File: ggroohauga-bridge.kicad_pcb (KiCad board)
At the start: 2 copper layers, 98.5 x 31 mm, 11 parts

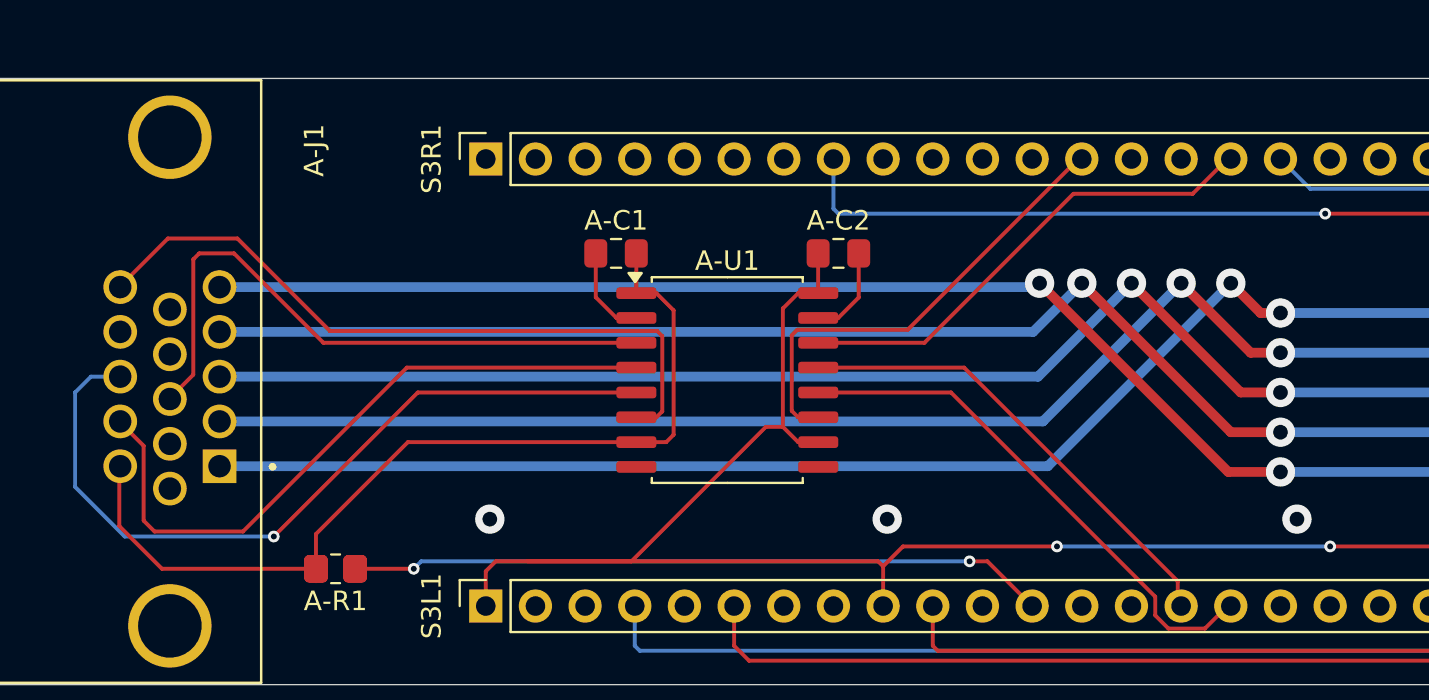
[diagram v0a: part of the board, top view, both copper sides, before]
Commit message: Add pull-up resistors to amplifier detect and RX inputs
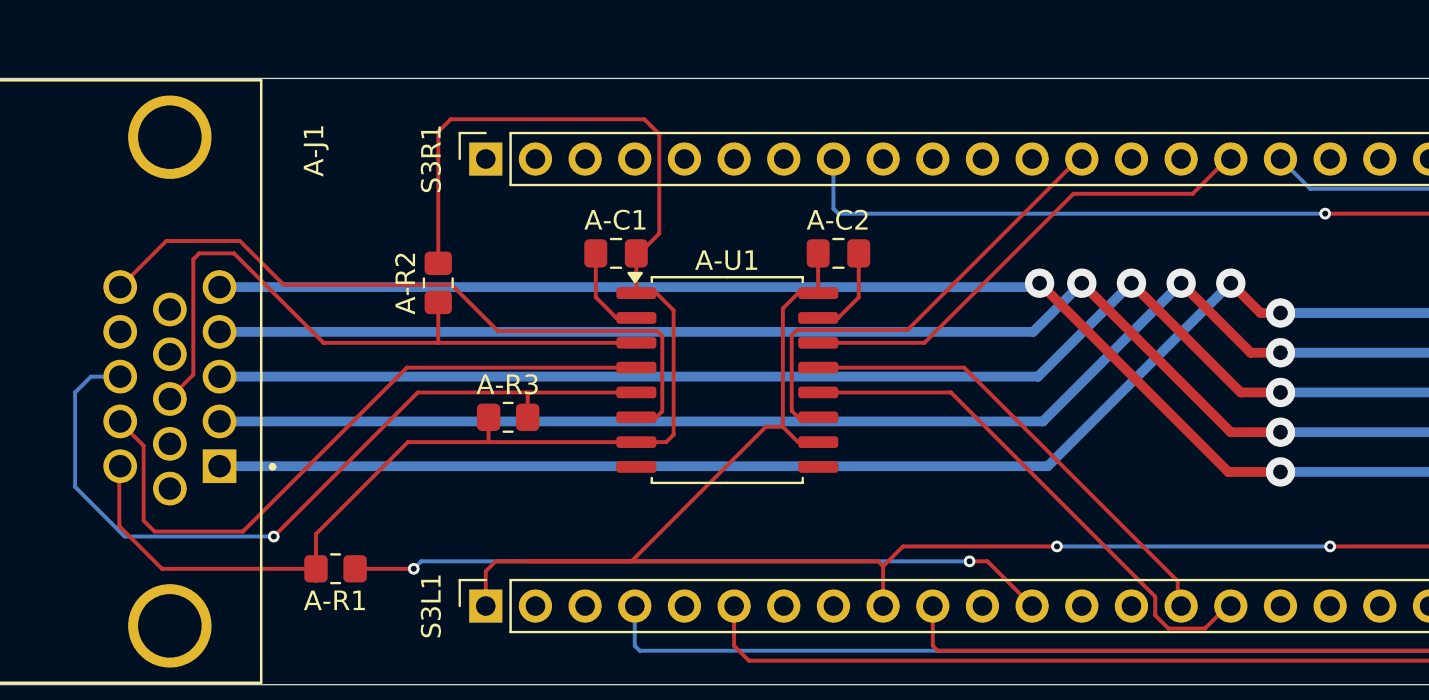
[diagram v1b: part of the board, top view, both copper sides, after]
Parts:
- removed ? (x2): , 
- added A-R2: 10kΩ, Resistor_SMD:R_0805_2012Metric_Pad1.20x1.40mm_HandSolder, F.Cu at (79.1, 60.9)
- added A-R3: 10kΩ, Resistor_SMD:R_0805_2012Metric_Pad1.20x1.40mm_HandSolder, F.Cu at (82.7, 67.8)
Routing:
- net /Common/AMP_POWER_IN: track 47.5 -> 73.9 mm
- net /Common/AMP_DETECT: track 32.3 -> 34.4 mm
- net /Common/AMP_RX: track 40.2 -> 41.5 mm
- net GND: vias 3 -> 0

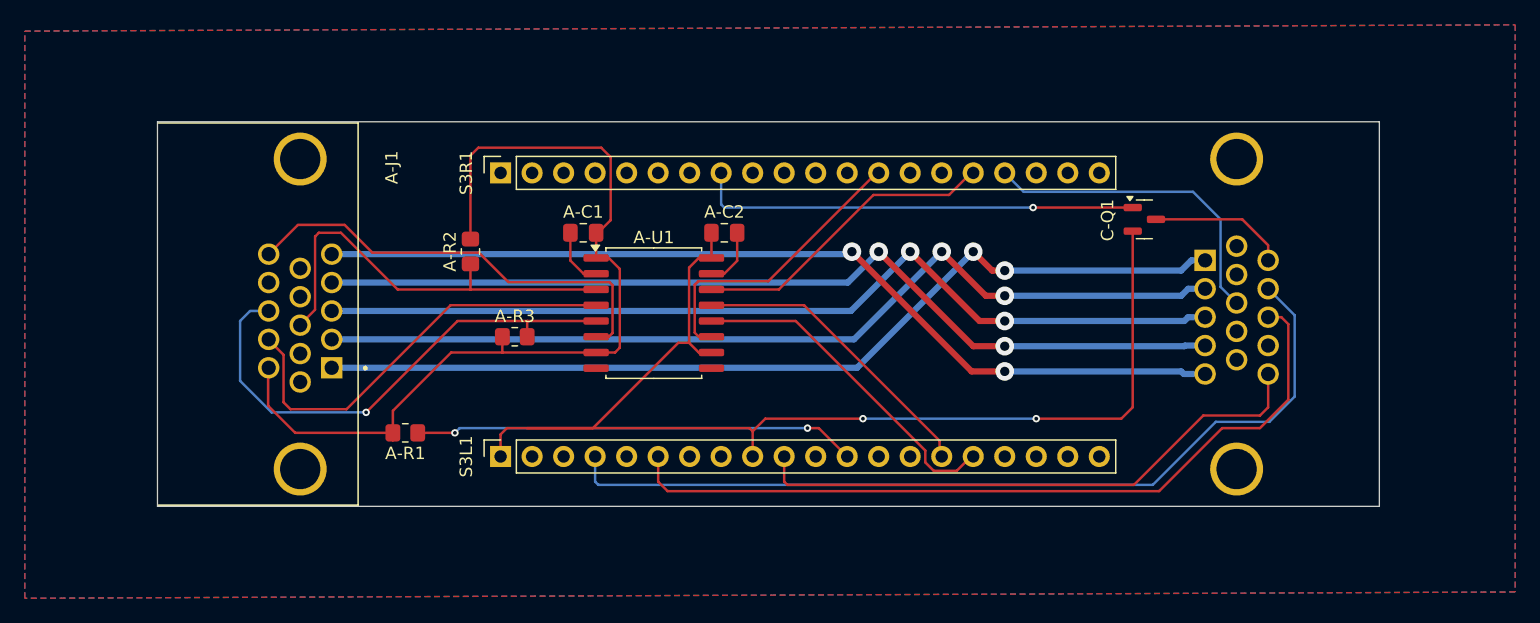
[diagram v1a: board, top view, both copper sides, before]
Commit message: Use consistent position of audio vias and rear silkscreen
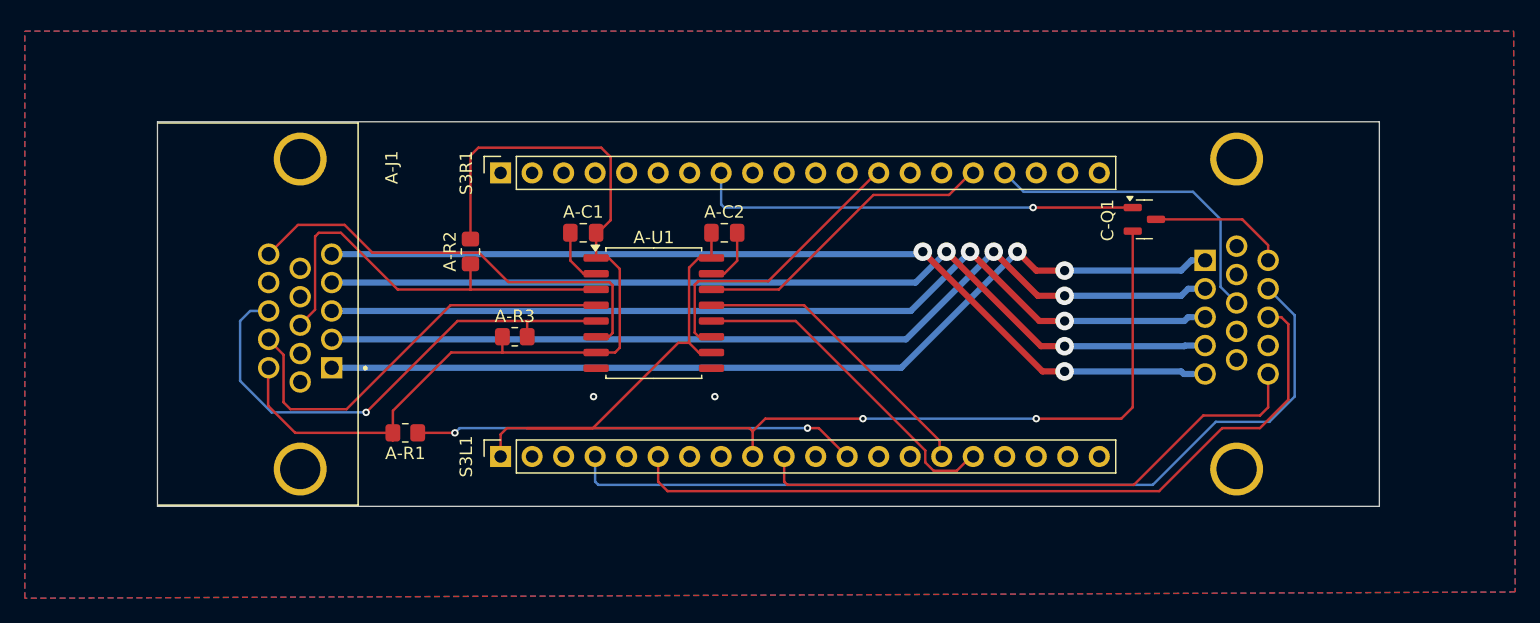
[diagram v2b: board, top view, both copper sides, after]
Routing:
- net GND: vias 0 -> 2
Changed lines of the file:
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@@
 	)
 	(gr_text "JLCJLCJLCJLC"
-		(at 132.366 58.42 90)
+		(at 134.144 58.42 90)
 		(layer "B.SilkS")
 		(effects
@@
 	)
 	(gr_text "urn:oid:1.3.6.1.4.1.39777.1.3.1.3.3\nhttps://github.com/nomis/ggroohauga-pcb\n(bridge)\n"
-		(at 120.65 66.04 0)
+		(at 123.825 66.04 0)
 		(layer "B.SilkS")
 		(effects
@@
 	)
 	(segment
-		(start 112.014 60.96)
-		(end 119.634 68.58)
+		(start 125.095 68.58)
+		(end 117.475 60.96)
 		(width 0.5)
 		(layer "F.Cu")
@@
 	)
 	(segment
-		(start 119.634 68.58)
-		(end 122.174 68.58)
+		(start 127 68.58)
+		(end 125.095 68.58)
 		(width 0.5)
 		(layer "F.Cu")
@@
 	)
 	(via
-		(at 122.174 68.58)
+		(at 127 68.58)
 		(size 1.5)
 		(drill 0.75)
@@
 	)
 	(via
-		(at 112.014 60.96)
+		(at 117.475 60.96)
 		(size 1.5)
 		(drill 0.75)
@@
 	)
 	(segment
-		(start 112.014 60.96)
-		(end 109.5248 63.4492)
-		(width 0.5)
-		(layer "B.Cu")
-		(net 2)
-	)
-	(segment
-		(start 122.174 68.58)
-		(end 136.652 68.58)
-		(width 0.5)
-		(layer "B.Cu")
-		(net 2)
-	)
-	(segment
-		(start 109.5248 63.4492)
-		(end 67.9196 63.4492)
+		(start 136.7028 68.5292)
+		(end 138.3272 68.5292)
 		(width 0.5)
 		(layer "B.Cu")
@@
 	)
 	(segment
-		(start 136.7028 68.5292)
-		(end 138.3272 68.5292)
+		(start 114.9858 63.4492)
+		(end 67.9196 63.4492)
+		(width 0.5)
+		(layer "B.Cu")
+		(net 2)
+	)
+	(segment
+		(start 117.475 60.96)
+		(end 114.9858 63.4492)
+		(width 0.5)
+		(layer "B.Cu")
+		(net 2)
+	)
+	(segment
+		(start 127 68.58)
+		(end 136.652 68.58)
 		(width 0.5)
 		(layer "B.Cu")
@@
 	)
 	(segment
-		(start 109.855 60.96)
-		(end 119.507 70.612)
+		(start 127 70.612)
+		(end 125.222 70.612)
 		(width 0.5)
 		(layer "F.Cu")
@@
 	)
 	(segment
-		(start 119.507 70.612)
-		(end 122.174 70.612)
+		(start 125.222 70.612)
+		(end 115.57 60.96)
 		(width 0.5)
 		(layer "F.Cu")
@@
 	)
 	(via
-		(at 122.174 70.612)
+		(at 127 70.612)
 		(size 1.5)
 		(drill 0.75)
@@
 	)
 	(via
-		(at 109.855 60.96)
+		(at 115.57 60.96)
 		(size 1.5)
 		(drill 0.75)
@@
 	)
 	(segment
+		(start 136.6052 70.8192)
+		(end 138.3272 70.8192)
+		(width 0.5)
+		(layer "B.Cu")
+		(net 8)
+	)
+	(segment
+		(start 127 70.612)
+		(end 136.398 70.612)
+		(width 0.5)
+		(layer "B.Cu")
+		(net 8)
+	)
+	(segment
+		(start 115.3708 61.1592)
+		(end 115.57 60.96)
+		(width 0.5)
+		(layer "B.Cu")
+		(net 8)
+	)
+	(segment
+		(start 67.9196 61.1592)
+		(end 115.3708 61.1592)
+		(width 0.5)
+		(layer "B.Cu")
+		(net 8)
+	)
+	(segment
 		(start 136.398 70.612)
 		(end 136.6052 70.8192)
@@
 	)
 	(segment
-		(start 136.6052 70.8192)
-		(end 138.3272 70.8192)
-		(width 0.5)
-		(layer "B.Cu")
-		(net 8)
-	)
-	(segment
-		(start 109.6558 61.1592)
-		(end 109.855 60.96)
-		(width 0.5)
-		(layer "B.Cu")
-		(net 8)
-	)
-	(segment
-		(start 122.174 70.612)
-		(end 136.398 70.612)
-		(width 0.5)
-		(layer "B.Cu")
-		(net 8)
-	)
-	(segment
-		(start 67.9196 61.1592)
-		(end 109.6558 61.1592)
-		(width 0.5)
-		(layer "B.Cu")
-		(net 8)
-	)
-	(segment
-		(start 119.634 60.96)
-		(end 121.158 62.484)
+		(start 127 62.484)
+		(end 124.714 62.484)
 		(width 0.5)
 		(layer "F.Cu")
@@
 	)
 	(segment
-		(start 121.158 62.484)
-		(end 122.174 62.484)
+		(start 124.714 62.484)
+		(end 123.19 60.96)
 		(width 0.5)
 		(layer "F.Cu")
@@
 	)
 	(via
-		(at 119.634 60.96)
+		(at 123.19 60.96)
 		(size 1.5)
 		(drill 0.75)
@@
 	)
 	(via
-		(at 122.174 62.484)
+		(at 127 62.484)
 		(size 1.5)
 		(drill 0.75)
@@
 	)
 	(segment
+		(start 123.19 60.96)
+		(end 113.8308 70.3192)
+		(width 0.5)
+		(layer "B.Cu")
+		(net 9)
+	)
+	(segment
 		(start 137.2228 61.6592)
-		(end 136.398 62.484)
+		(end 138.3272 61.6592)
 		(width 0.5)
 		(layer "B.Cu")
@@
 	)
 	(segment
-		(start 119.634 60.96)
-		(end 110.2748 70.3192)
+		(start 113.8308 70.3192)
+		(end 67.9196 70.3192)
 		(width 0.5)
 		(layer "B.Cu")
@@
 	)
 	(segment
-		(start 138.3272 61.6592)
+		(start 136.398 62.484)
 		(end 137.2228 61.6592)
 		(width 0.5)
@@
 	)
 	(segment
-		(start 110.2748 70.3192)
-		(end 67.9196 70.3192)
+		(start 136.398 62.484)
+		(end 127 62.484)
 		(width 0.5)
 		(layer "B.Cu")
@@
 	)
 	(segment
-		(start 136.398 62.484)
-		(end 122.174 62.484)
-		(width 0.5)
-		(layer "B.Cu")
-		(net 9)
-	)
-	(segment
-		(start 120.142 66.548)
-		(end 122.174 66.548)
+		(start 127 66.548)
+		(end 124.968 66.548)
 		(width 0.5)
 		(layer "F.Cu")
@@
 	)
 	(segment
-		(start 114.554 60.96)
-		(end 120.142 66.548)
+		(start 124.968 66.548)
+		(end 119.38 60.96)
 		(width 0.5)
 		(layer "F.Cu")
@@
 	)
 	(via
-		(at 114.554 60.96)
+		(at 119.38 60.96)
 		(size 1.5)
 		(drill 0.75)
@@
 	)
 	(via
-		(at 122.174 66.548)
+		(at 127 66.548)
 		(size 1.5)
 		(drill 0.75)
@@
 	)
 	(segment
-		(start 122.174 66.548)
+		(start 119.38 60.96)
+		(end 114.6008 65.7392)
+		(width 0.5)
+		(layer "B.Cu")
+		(net 10)
+	)
+	(segment
+		(start 136.652 66.548)
+		(end 136.9608 66.2392)
+		(width 0.5)
+		(layer "B.Cu")
+		(net 10)
+	)
+	(segment
+		(start 114.6008 65.7392)
+		(end 67.9196 65.7392)
+		(width 0.5)
+		(layer "B.Cu")
+		(net 10)
+	)
+	(segment
+		(start 127 66.548)
 		(end 136.652 66.548)
 		(width 0.5)
@@
 	)
 	(segment
-		(start 109.7748 65.7392)
-		(end 67.9196 65.7392)
-		(width 0.5)
-		(layer "B.Cu")
-		(net 10)
-	)
-	(segment
-		(start 114.554 60.96)
-		(end 109.7748 65.7392)
-		(width 0.5)
-		(layer "B.Cu")
-		(net 10)
-	)
-	(segment
-		(start 136.652 66.548)
-		(end 136.9608 66.2392)
-		(width 0.5)
-		(layer "B.Cu")
-		(net 10)
-	)
-	(segment
-		(start 117.094 60.96)
-		(end 120.65 64.516)
+		(start 127 64.516)
+		(end 124.841 64.516)
 		(width 0.5)
 		(layer "F.Cu")
@@
 	)
 	(segment
-		(start 120.65 64.516)
-		(end 122.174 64.516)
+		(start 124.841 64.516)
+		(end 121.285 60.96)
 		(width 0.5)
 		(layer "F.Cu")
@@
 	)
 	(via
-		(at 117.094 60.96)
+		(at 121.285 60.96)
 		(size 1.5)
 		(drill 0.75)
@@
 	)
 	(via
-		(at 122.174 64.516)
+		(at 127 64.516)
 		(size 1.5)
 		(drill 0.75)
@@
 	)
 	(segment
+		(start 136.9648 63.9492)
+		(end 138.3272 63.9492)
+		(width 0.5)
+		(layer "B.Cu")
+		(net 14)
+	)
+	(segment
+		(start 121.285 60.96)
+		(end 114.2158 68.0292)
+		(width 0.5)
+		(layer "B.Cu")
+		(net 14)
+	)
+	(segment
+		(start 114.2158 68.0292)
+		(end 67.9196 68.0292)
+		(width 0.5)
+		(layer "B.Cu")
+		(net 14)
+	)
+	(segment
 		(start 136.398 64.516)
 		(end 136.9648 63.9492)
@@
 	)
 	(segment
-		(start 110.0248 68.0292)
-		(end 67.9196 68.0292)
-		(width 0.5)
-		(layer "B.Cu")
-		(net 14)
-	)
-	(segment
-		(start 122.174 64.516)
+		(start 127 64.516)
 		(end 136.398 64.516)
-		(width 0.5)
-		(layer "B.Cu")
-		(net 14)
-	)
-	(segment
-		(start 117.094 60.96)
-		(end 110.0248 68.0292)
-		(width 0.5)
-		(layer "B.Cu")
-		(net 14)
-	)
-	(segment
-		(start 136.9648 63.9492)
-		(end 138.3272 63.9492)
 		(width 0.5)
 		(layer "B.Cu")
@@
 		(width 0.2)
 		(layer "F.Cu")
+		(net 36)
+	)
+	(via
+		(at 98.806 72.644)
+		(size 0.6)
+		(drill 0.3)
+		(layers "F.Cu" "B.Cu")
+		(free yes)
+		(net 36)
+	)
+	(via
+		(at 89.027 72.644)
+		(size 0.6)
+		(drill 0.3)
+		(layers "F.Cu" "B.Cu")
+		(free yes)
 		(net 36)
 	)
@@
 		(polygon
 			(pts
-				(xy 43.18 43.18) (xy 163.322 42.672) (xy 163.322 88.392) (xy 43.18 88.9)
+				(xy 43.18 43.18) (xy 163.195 43.18) (xy 163.322 88.392) (xy 43.18 88.9)
 			)
 		)

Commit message: Add "music with rocks in" image
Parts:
- added MUSICWITHROCKSIN: LOGO, LOGO, B.Cu at (81.3, 64.5)

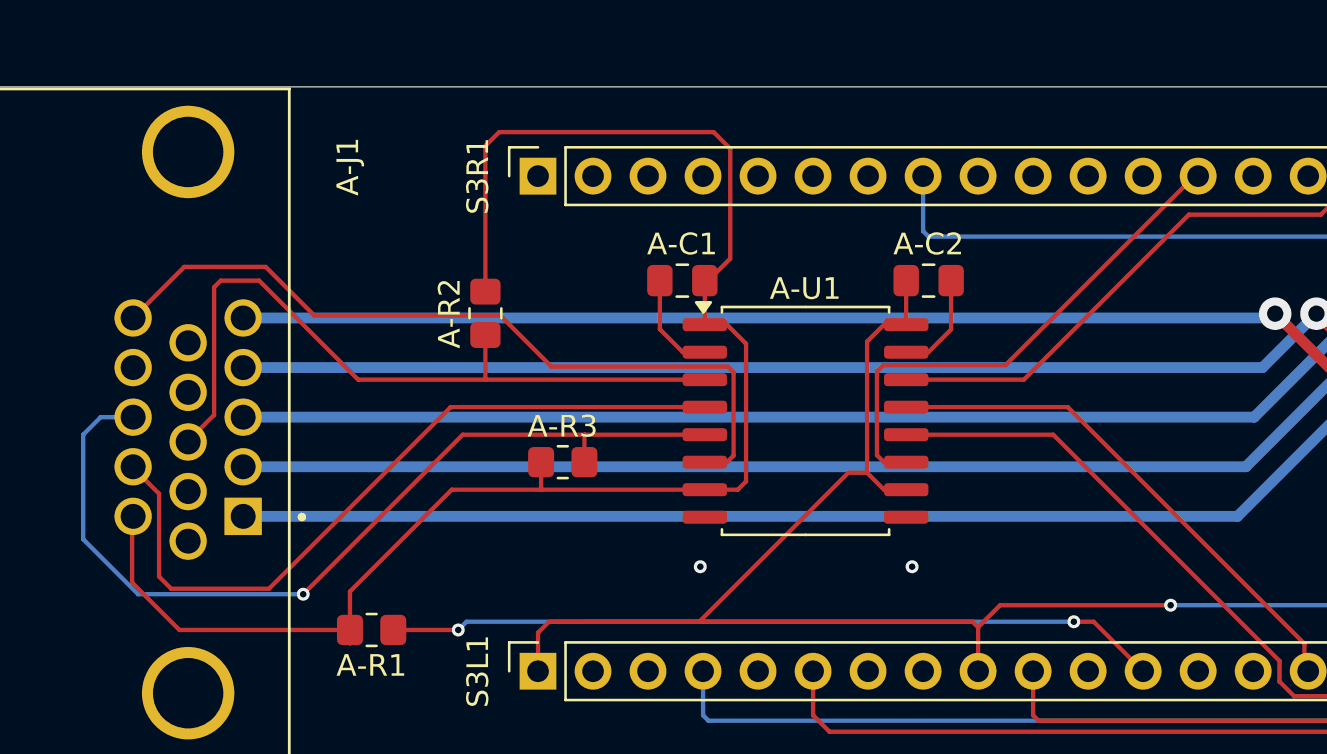
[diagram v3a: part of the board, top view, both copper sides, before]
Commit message: Realign amplifier and bridge PCBs so that they match
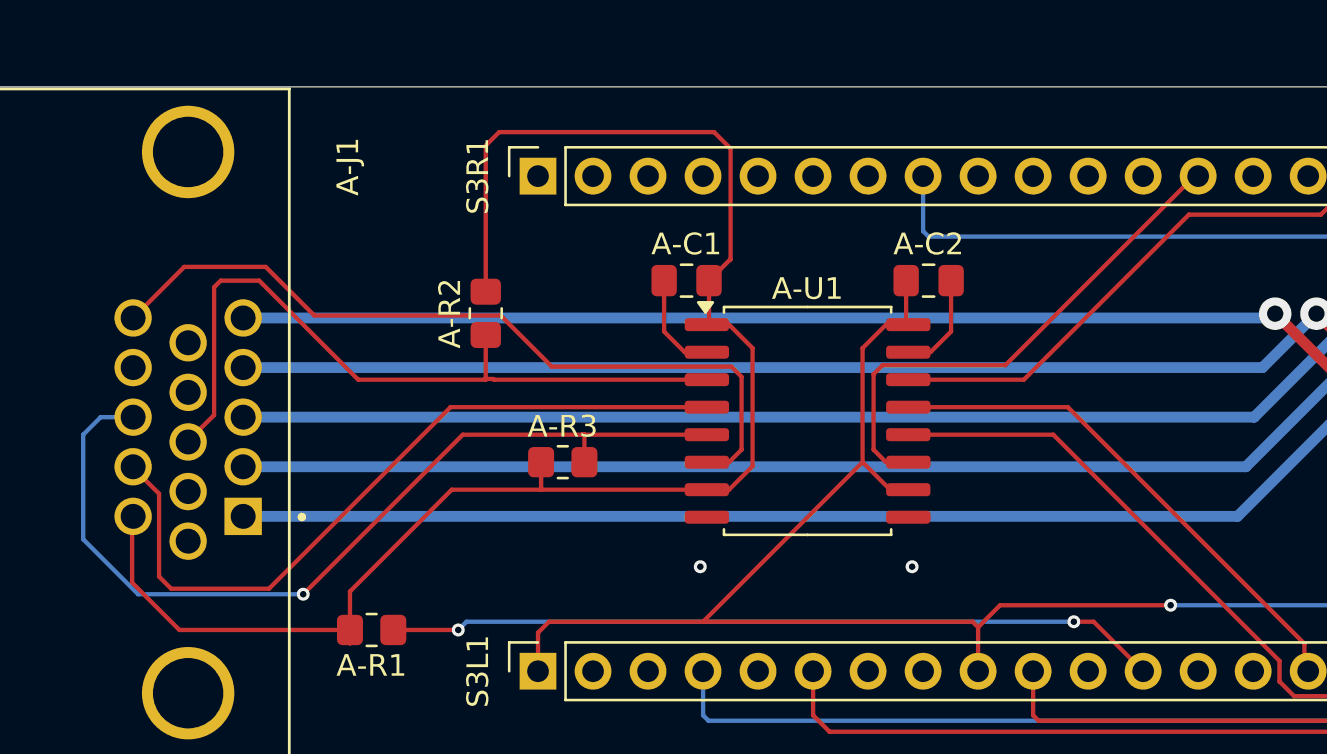
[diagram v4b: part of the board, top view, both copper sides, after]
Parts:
- moved A-C1 0.20 mm to (88.4, 59.4)
- moved A-U1 0.10 mm to (94.0, 65.9)
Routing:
- net +3.3V: track 98.4 -> 92.1 mm
- net /Common/AMP_POWER_IN: track 73.9 -> 74.8 mm

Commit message: Fix thin lines in image
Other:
- board text added: "https://github.com/nomis/ggroohauga-pcb (bridge)"
- board text added: "urn:oid:1.3.6.1.4.1.39777.1.3.1.3.3"
- board text removed: "urn:oid:1.3.6.1.4.1.39777.1.3.1.3.3 https://github.com/nomis/ggroohauga-pcb (bridge)"
